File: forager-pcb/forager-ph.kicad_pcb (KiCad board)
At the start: 2 copper layers, 114.6 x 96.3 mm, 26 parts

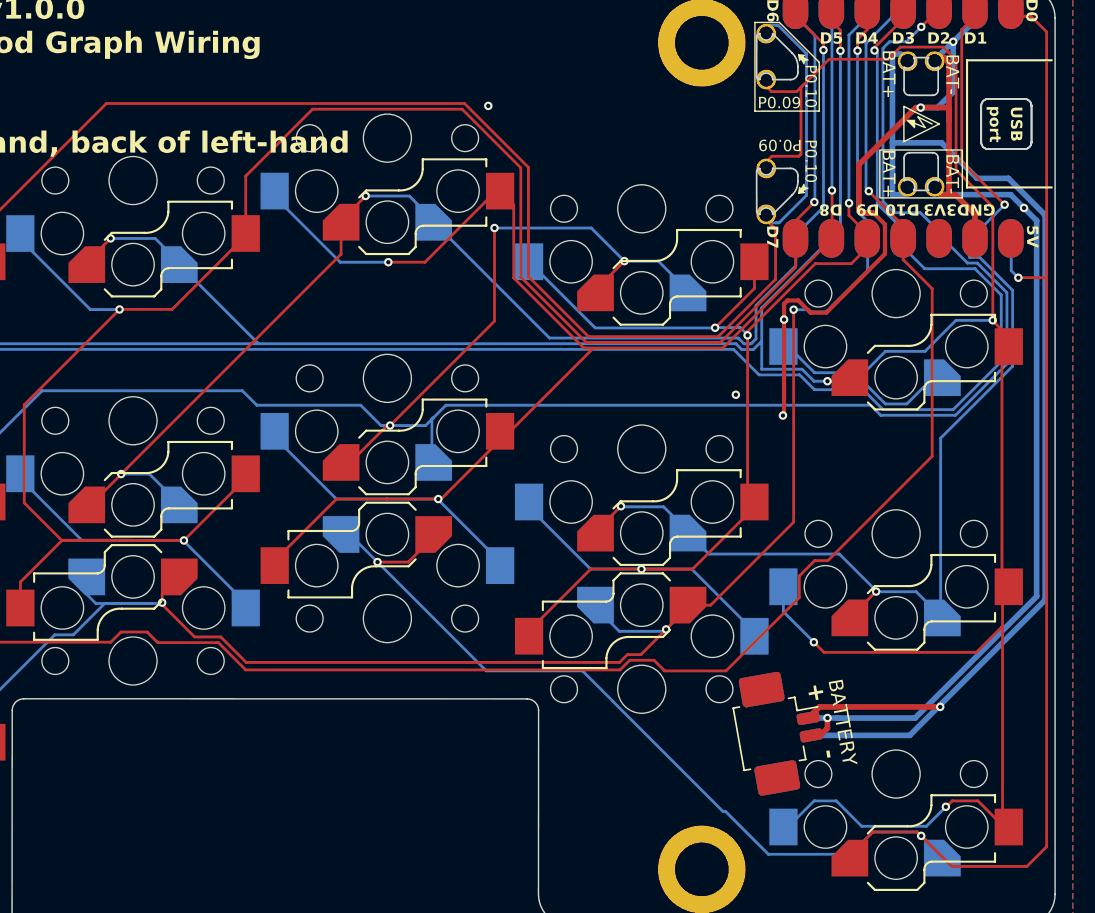
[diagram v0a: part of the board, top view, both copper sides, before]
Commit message: Restore direct solder points for battery connection
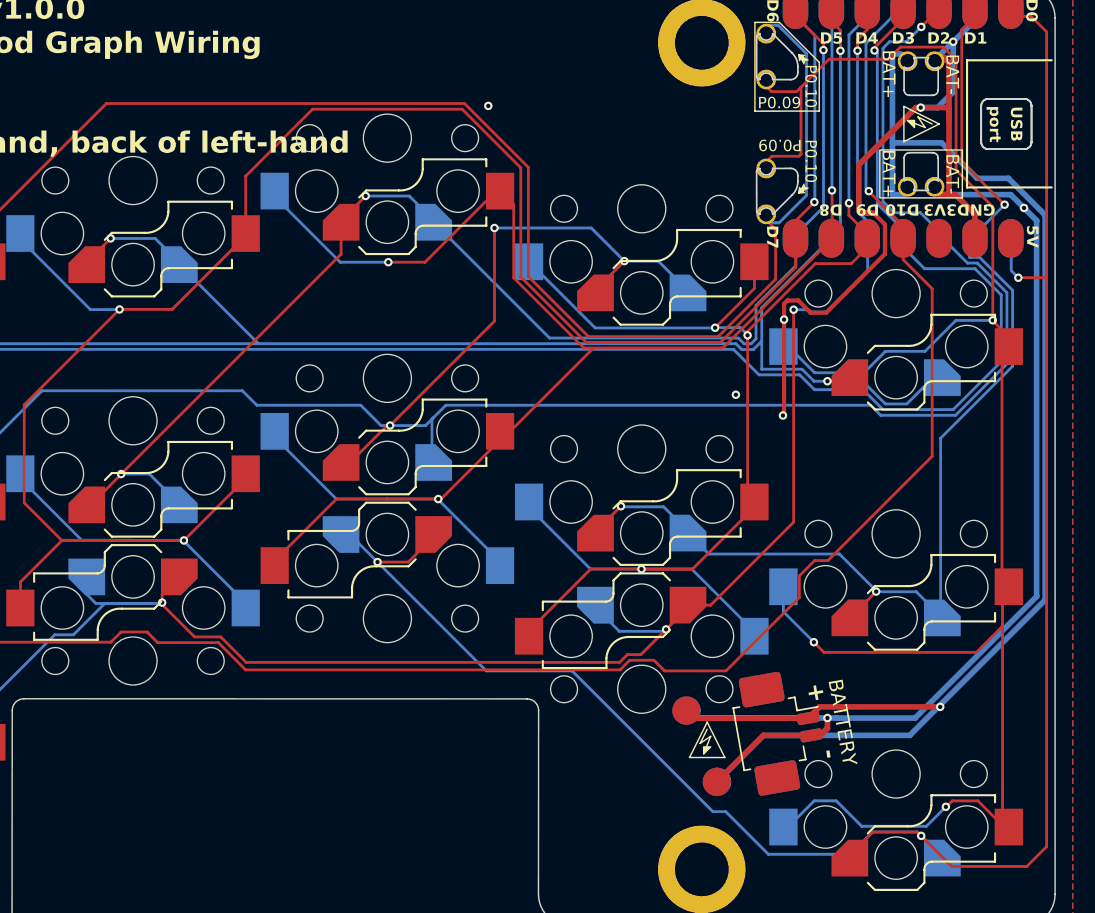
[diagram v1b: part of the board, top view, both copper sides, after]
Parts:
- added ?: , clipboard:c6e4976e-07e6-4aae-98ea-2f932d7c0aa1, F.Cu at (92.4, 4.83)
- added ?: , , B.Cu at (94.3, 6.56)
- added ?: , clipboard:c6e4976e-07e6-4aae-98ea-2f932d7c0aa1, B.Cu at (94.9, 4.84)
- added ?: , , B.Cu at (92.2, 1.51)
- added TP1: TestPoint, TestPoint:TestPoint_Pad_D2.0mm, B.Cu at (94.3, 6.55)
- added TP2: TestPoint, TestPoint:TestPoint_Pad_D2.0mm, B.Cu at (92.2, 1.51)
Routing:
- net GND: track 114.0 -> 131.5 mm
- net BAT: track 81.8 -> 98.0 mm
- net C4: track 133.3 -> 130.7 mm
- net C2: track 116.6 -> 115.7 mm

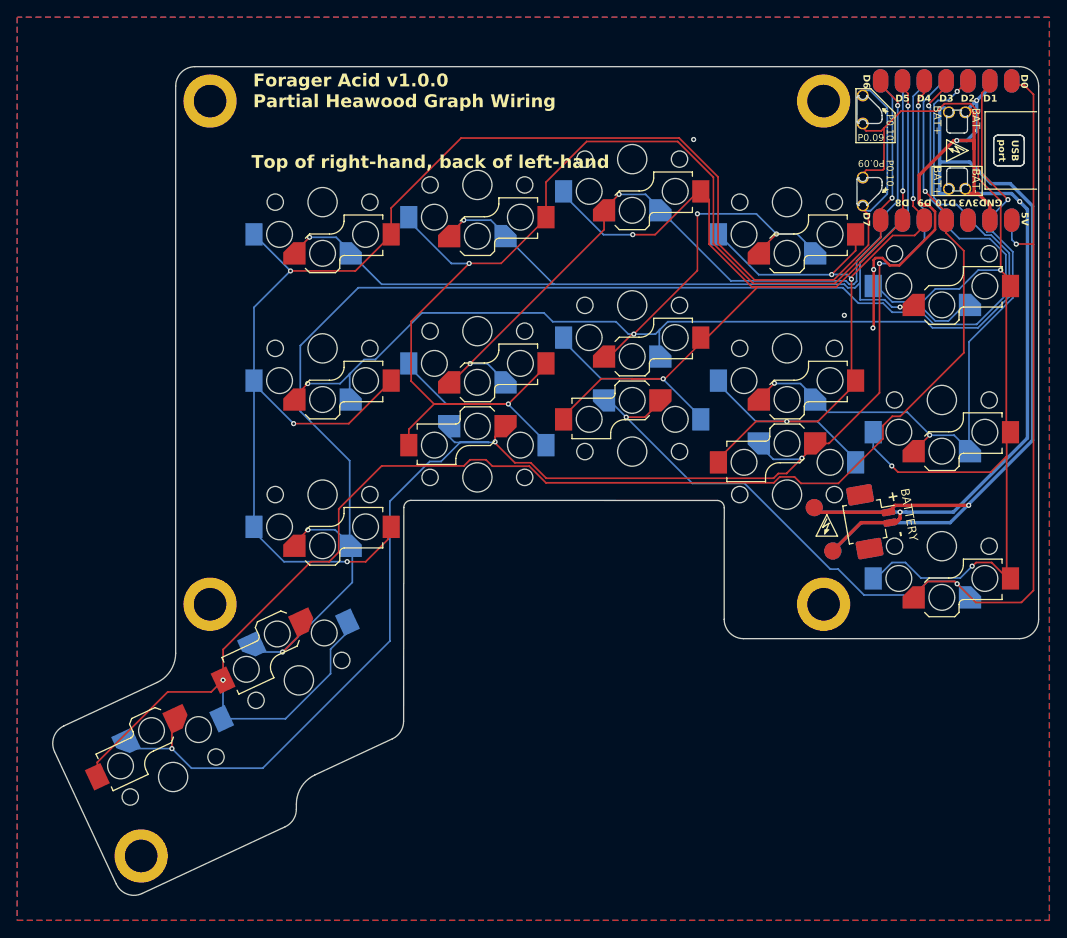
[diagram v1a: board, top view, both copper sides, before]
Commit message: Add bonus sideways SMD thumb switch to fill out the matrix.
This will need a tiny case mode, and perhaps a longer than usual button
if this isn't close enough to the edge? Vertical position limited by
bottom case rib.

Wiring required a few more vias for the ground plane.
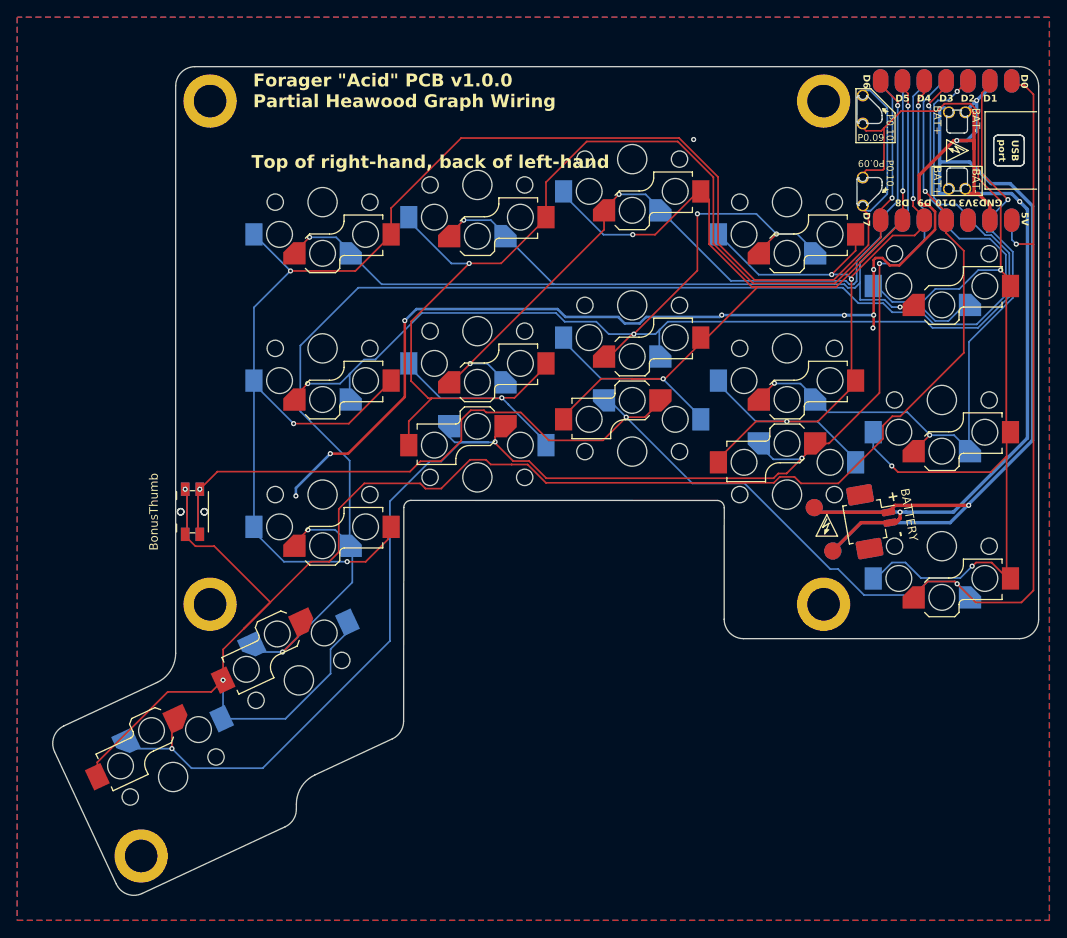
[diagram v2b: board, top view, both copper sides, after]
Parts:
- added BonusThumb: Panasonic_EVQPUL_EVQPUC, Button_Switch_SMD:Panasonic_EVQPUL_EVQPUC, F.Cu at (19.9, 2.00)
- added BonusThumb: Panasonic_EVQPUL_EVQPUC, Button_Switch_SMD:Panasonic_EVQPUL_EVQPUC, B.Cu at (19.9, 2.00)
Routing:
- net GND: track 131.5 -> 215.3 mm, vias 8 -> 13
- net R4: track 139.0 -> 206.0 mm, vias 3 -> 4
- net C5: track 188.1 -> 215.7 mm, vias 2 -> 3
- net C1: track 165.2 -> 157.0 mm
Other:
- board text added: "Forager {dblquote}Acid{dblquote} PCB v1.0.0 Partial Heawood Graph Wiring"
- board text removed: "Forager Acid v1.0.0 Partial Heawood Graph Wiring"

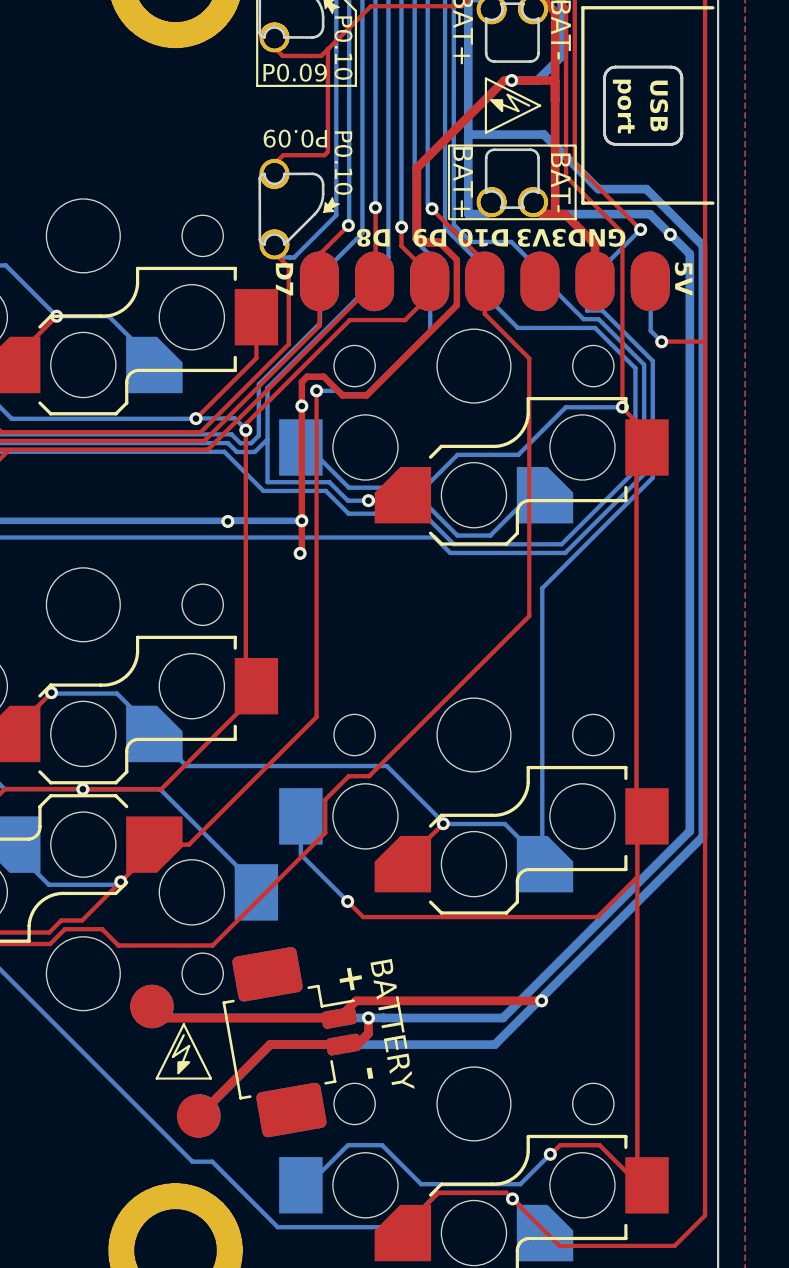
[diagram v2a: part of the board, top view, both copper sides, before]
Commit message: Change to thru-hole battery terminals for direct solder option
Hat tip https://github.com/letmegobacktosleep/forager/tree/power-switch/forager-pcb
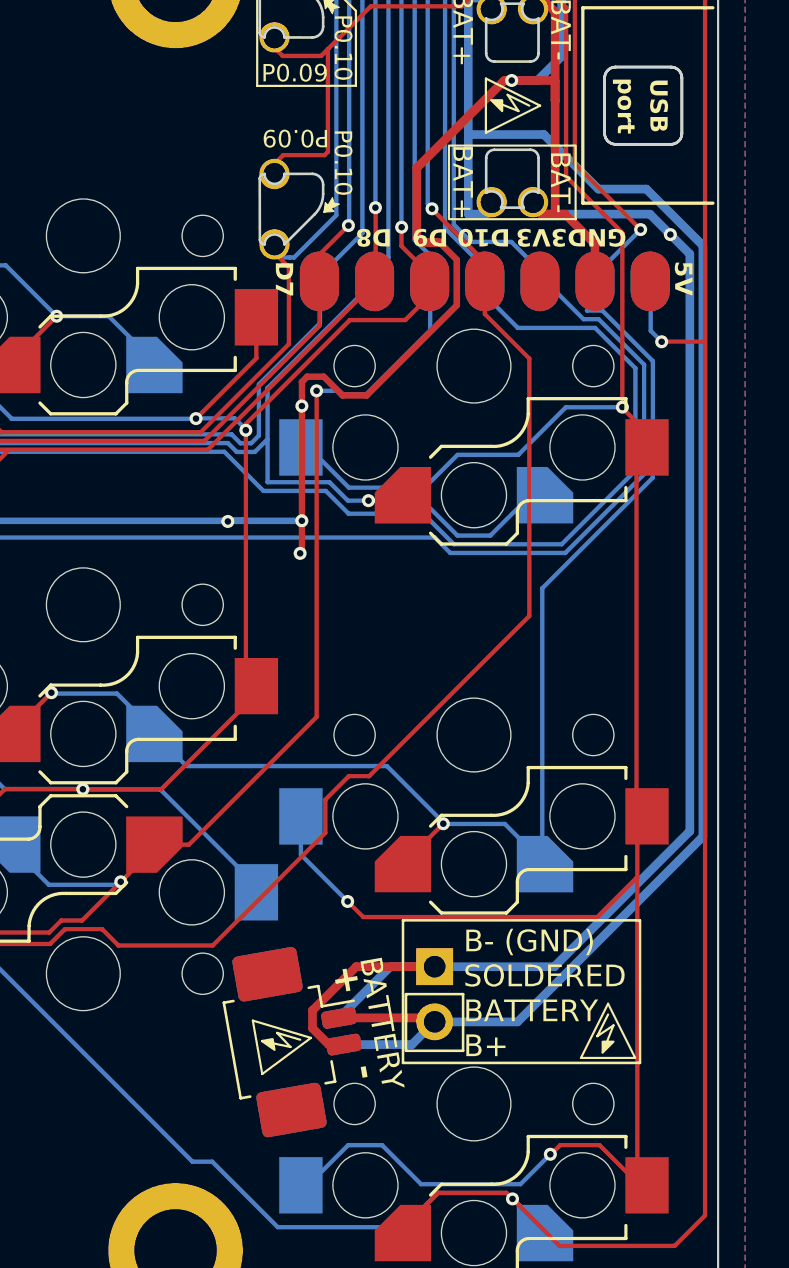
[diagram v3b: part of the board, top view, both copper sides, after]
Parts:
- removed the ? at (94.3, 6.56)
- removed the ? at (92.2, 1.51)
- removed TP1, TP2: TestPoint, TestPoint:TestPoint_Pad_D2.0mm
- added ?: , clipboard:c6e4976e-07e6-4aae-98ea-2f932d7c0aa1, F.Cu at (111.9, 3.88)
- added ?: , clipboard:c6e4976e-07e6-4aae-98ea-2f932d7c0aa1, B.Cu at (114.4, 3.89)
- added J4: Conn_01x02_Pin, Connector_PinHeader_2.54mm:PinHeader_1x02_P2.54mm_Vertical, B.Cu at (105.2, -0.33)
- moved ? 5.17 mm to (96.8, 2.16), turned to -80 degrees
- moved ? 2.36 mm to (97.2, 4.62), turned to 100 degrees
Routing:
- net BAT: track 98.0 -> 76.3 mm, vias 1 -> 0
- net GND: track 215.3 -> 204.8 mm, vias 13 -> 12
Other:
- board text added: "(GND) B- SOLDERED BATTERY B+"
- board text added: "B- (GND) SOLDERED BATTERY B+"

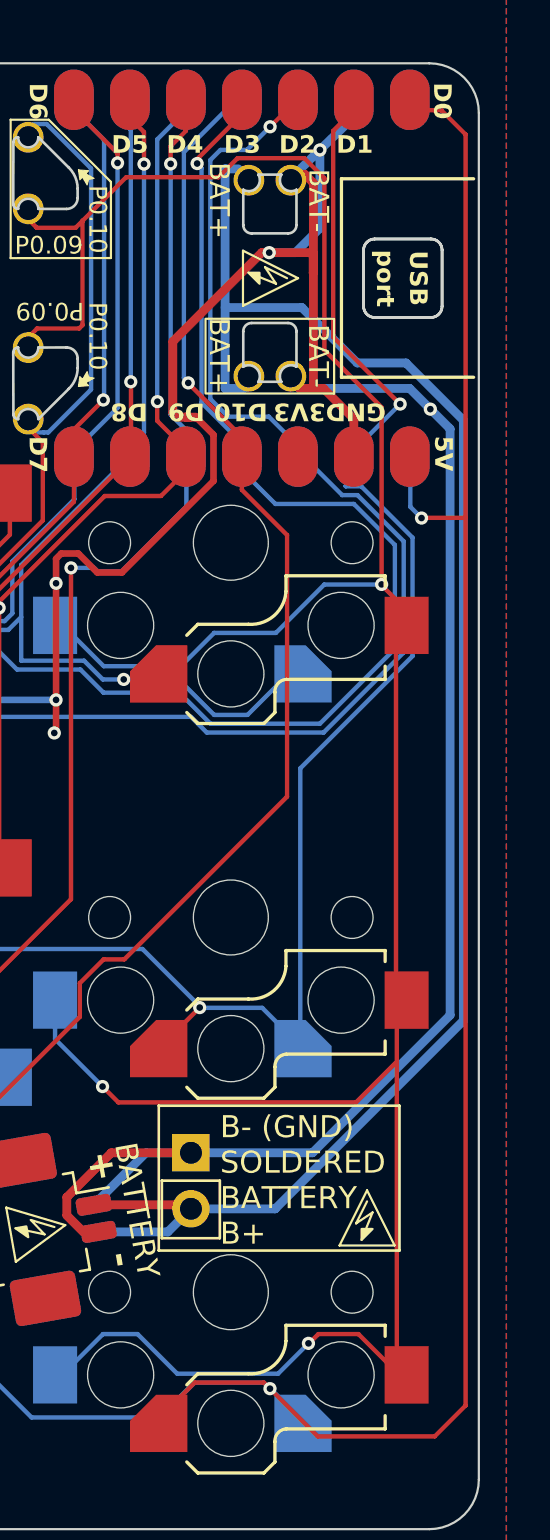
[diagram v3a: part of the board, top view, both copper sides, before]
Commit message: Add MSK12C02 power switch - LCSC C431540 or similar, SMD
These should both be up off (towards controller corner), and
down on (away from controller). Ought to be able to solder
bridge the pads if not using the switch?

Hat tip https://github.com/letmegobacktosleep/forager/tree/power-switch/forager-pcb
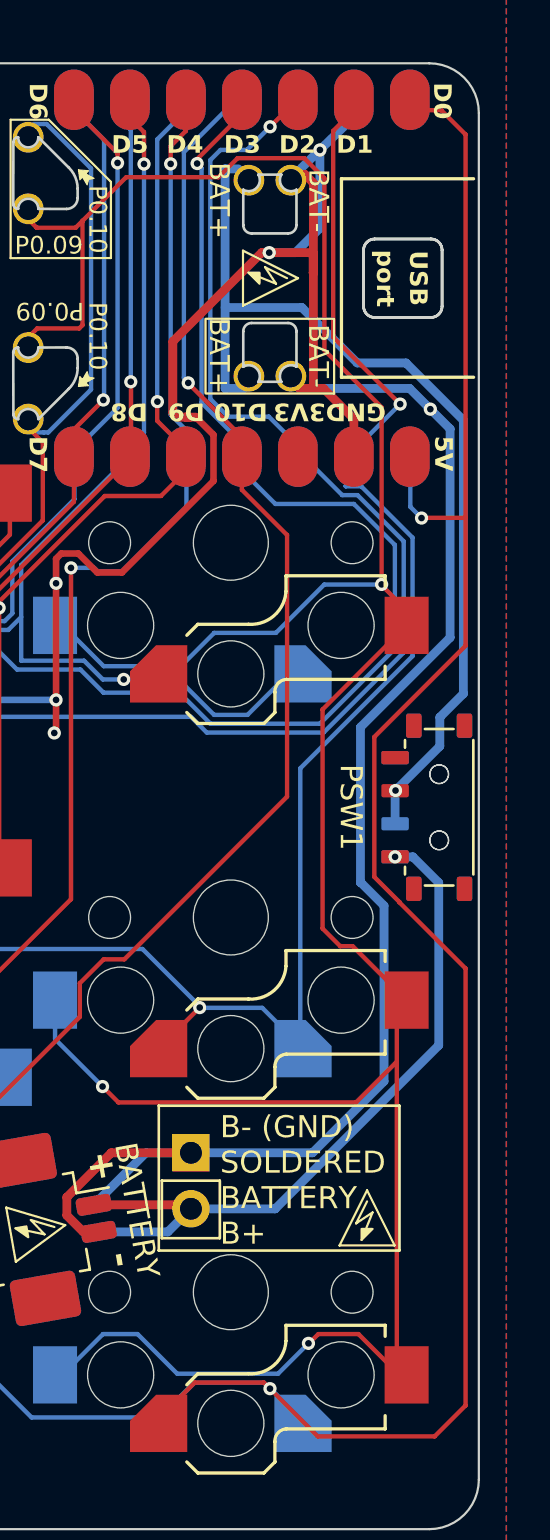
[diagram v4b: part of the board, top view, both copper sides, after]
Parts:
- added PSW1: SW_SPDT, PCM_marbastlib-various:SW_MSK12C02-HB, F.Cu at (116.5, -16.0)
- added PSW2: SW_SPDT, PCM_marbastlib-various:SW_MSK12C02-HB, B.Cu at (116.5, -16.0)
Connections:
- BAT pad 1: BAT -> BAT_CON
- BATTERY pad 1: BAT -> BAT_CON
- J4 pad 2: BAT -> BAT_CON
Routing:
- net BAT_CON: track 0.00 -> 33.0 mm, vias 0 -> 1
- net BAT: track 76.3 -> 43.9 mm, vias 0 -> 1
- net C4: track 130.7 -> 135.1 mm
- net R4: track 206.0 -> 209.5 mm
- net GND: track 204.8 -> 205.7 mm
